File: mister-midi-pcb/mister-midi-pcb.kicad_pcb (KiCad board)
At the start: 2 copper layers, 106.9 x 68.6 mm, 31 parts, among them J1 Midi In, J2 USB3_A, J3 Midi Out, J4 Midi Thru, U1 H11L1, U2 74HC14, U3 LM1117-3.3

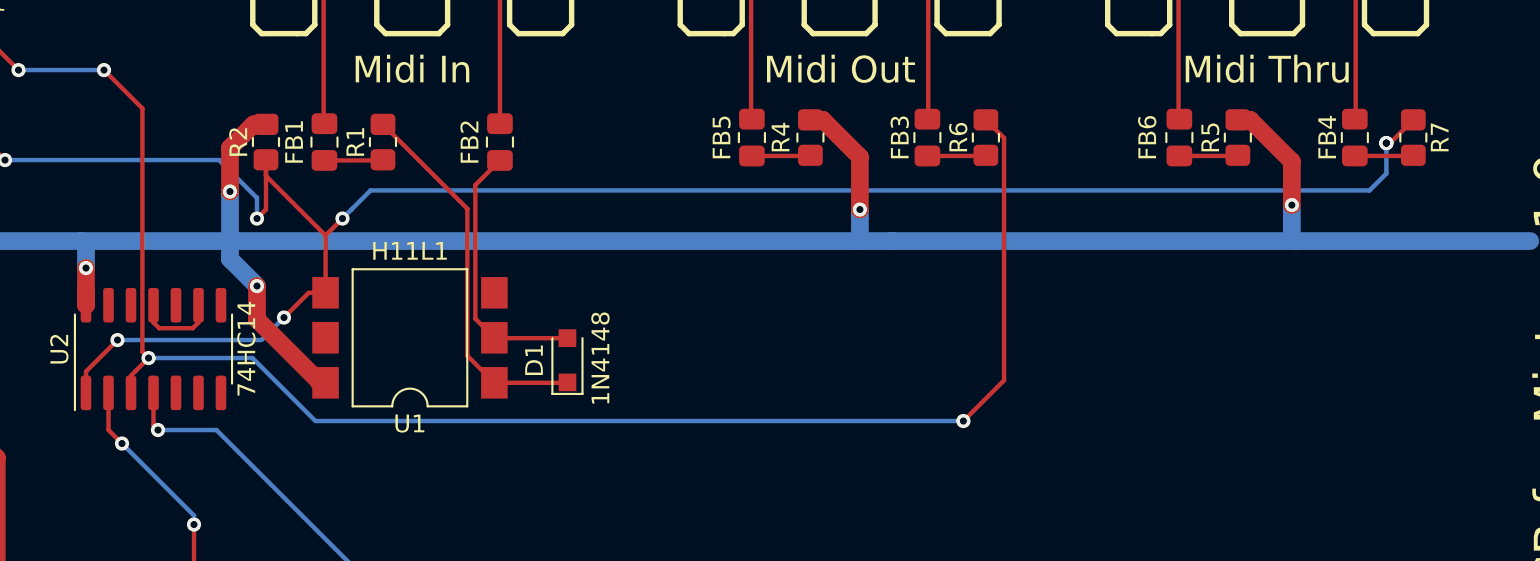
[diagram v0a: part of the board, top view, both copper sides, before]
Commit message: out and thru go through buffer now.
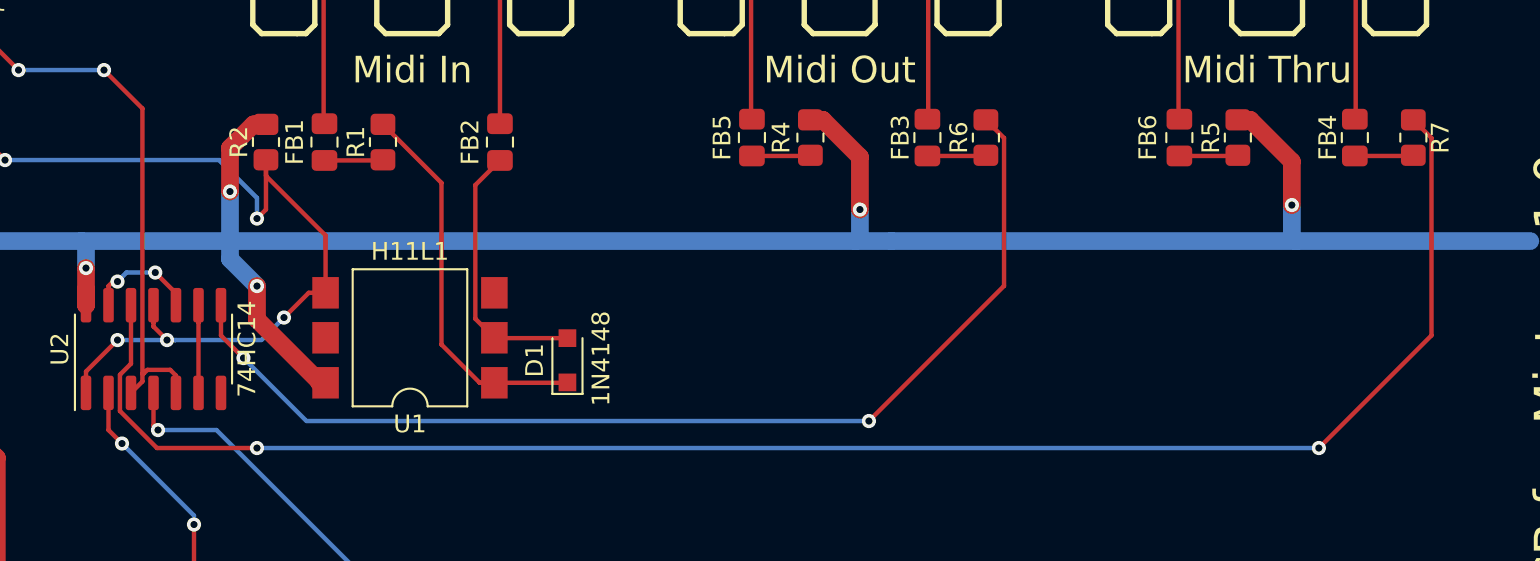
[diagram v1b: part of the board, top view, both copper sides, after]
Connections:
- R6 pad 1: Midi_Out_TX -> Net-(R6-Pad1)
- R7 pad 2: Midi_In_RX -> Net-(R7-Pad2)
- U2 pad 11: GND -> Midi_In_RX
- U2 pad 12: Net-(U2-Pad12) -> Net-(R7-Pad2)
- U2 pad 13: GND -> Net-(U2-Pad10)
- U2 pad 5: GND -> Midi_Out_TX
- U2 pad 8: Net-(U2-Pad8) -> Net-(R6-Pad1)
- U2 pad 9: GND -> Net-(U2-Pad6)
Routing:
- net Net-(R7-Pad2): track 0.00 -> 96.4 mm, vias 0 -> 2
- net Midi_Out_TX: track 101.0 -> 37.9 mm, vias 4 -> 2
- net Midi_In_RX: track 126.6 -> 65.2 mm, vias 7 -> 5
- net Net-(R6-Pad1): track 0.00 -> 60.9 mm, vias 0 -> 2
- net Net-(U2-Pad10): track 0.00 -> 7.19 mm, vias 0 -> 2
- net Net-(U2-Pad6): track 0.00 -> 5.92 mm
- net GND: track 4.76 -> 0.00 mm

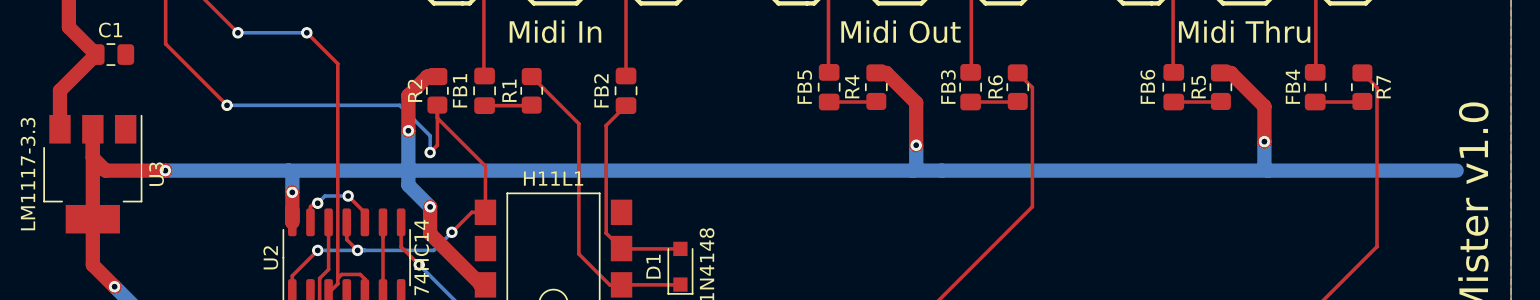
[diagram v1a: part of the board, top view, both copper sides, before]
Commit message: small trace improvements.
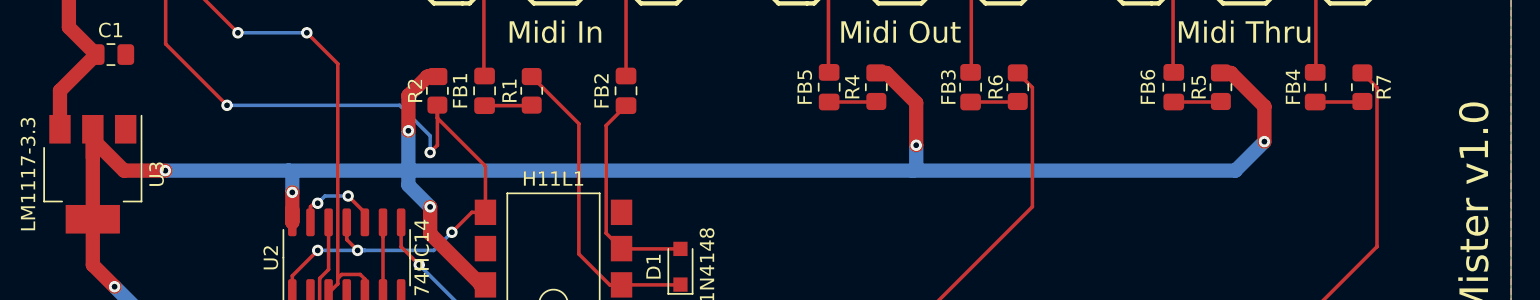
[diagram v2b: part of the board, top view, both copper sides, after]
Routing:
- net +3V3: track 182.0 -> 168.5 mm

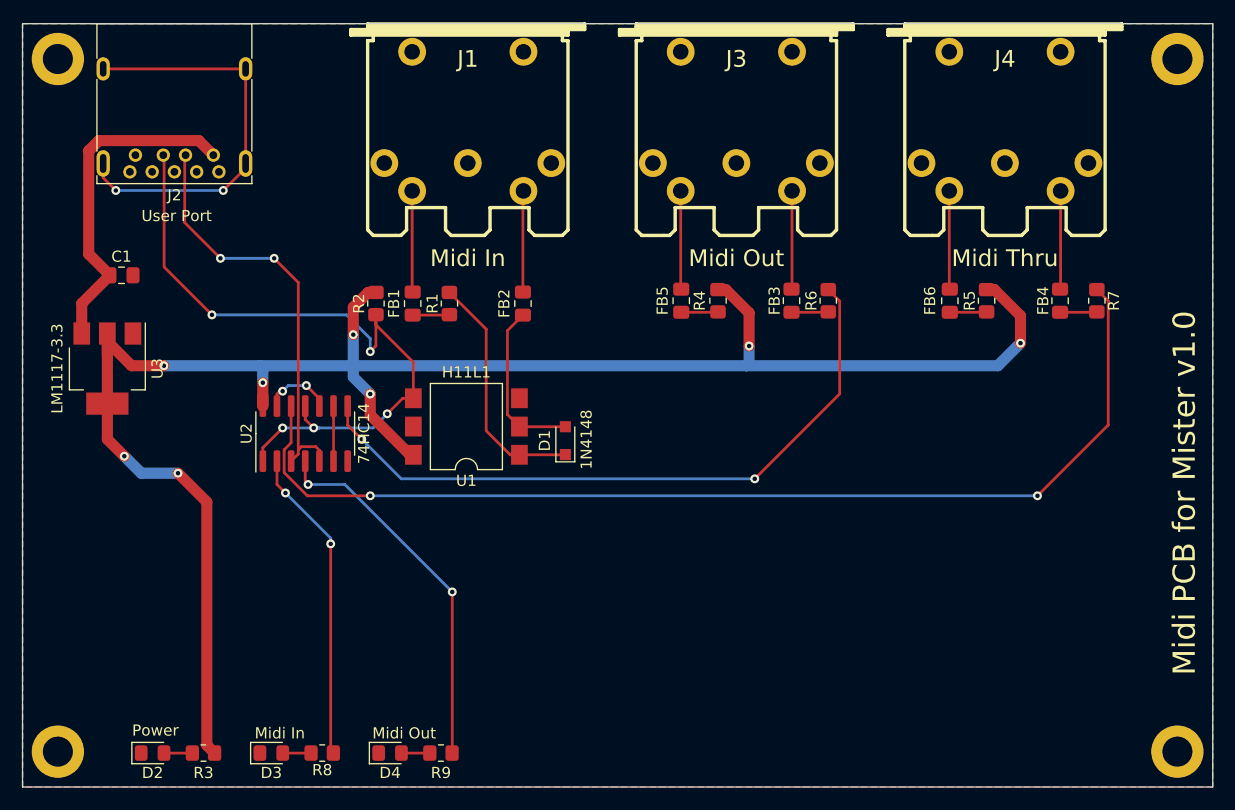
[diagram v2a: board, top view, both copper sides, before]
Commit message: added capacitors for ldo
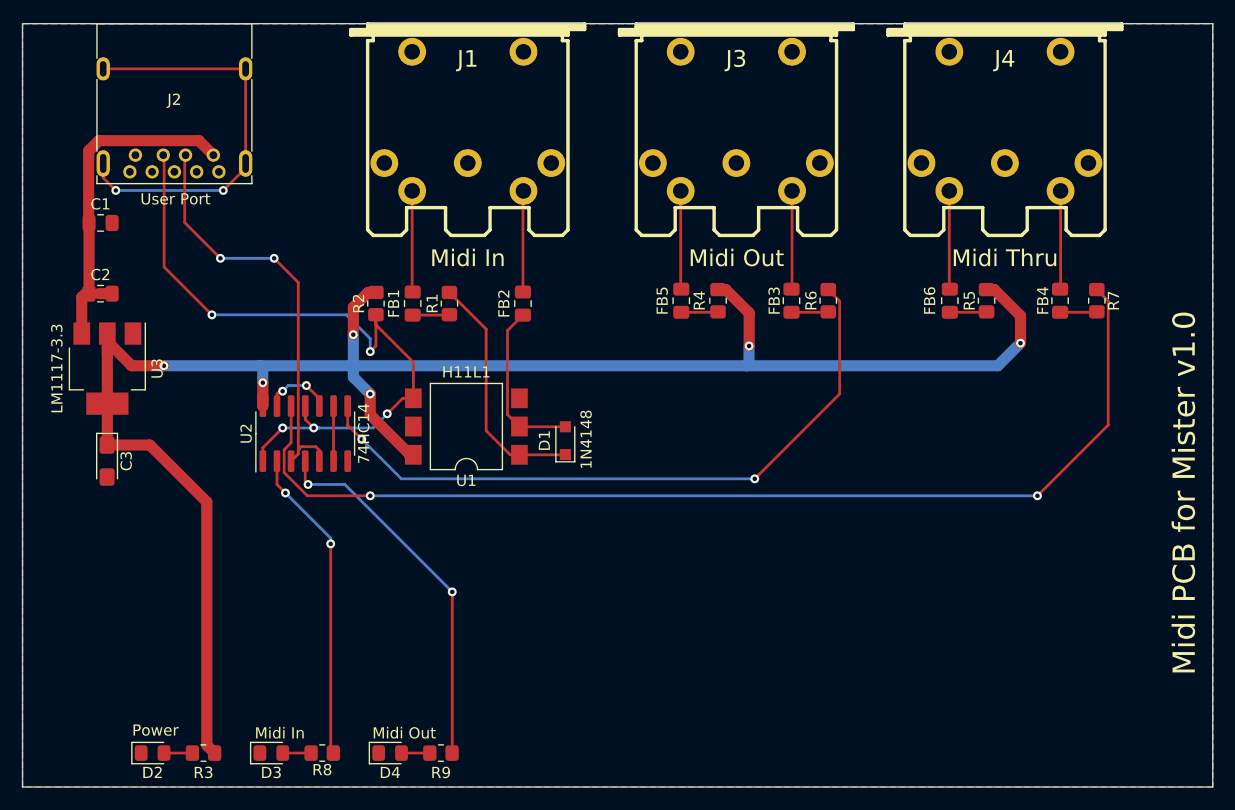
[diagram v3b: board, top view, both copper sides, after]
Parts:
- removed REF** (x4): MountingHole_2.7mm_M2.5_DIN965_Pad, MountingHole:MountingHole_2.7mm_M2.5_DIN965_Pad
- added C2: 10uF, Capacitor_SMD:C_0805_2012Metric_Pad1.18x1.45mm_HandSolder, F.Cu at (68.0, 100.5)
- added C3: 10uF, Capacitor_Tantalum_SMD:CP_EIA-3216-18_Kemet-A_Pad1.58x1.35mm_HandSolder, F.Cu at (68.6, 115.5)
- moved C1 5.06 mm to (68.0, 94.1)
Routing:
- net +5V: track 30.4 -> 27.8 mm
- net GND: track 0.00 -> 0.76 mm
- net +3V3: track 168.5 -> 168.8 mm, vias 8 -> 6

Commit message: updated gerbers, holes were missing.
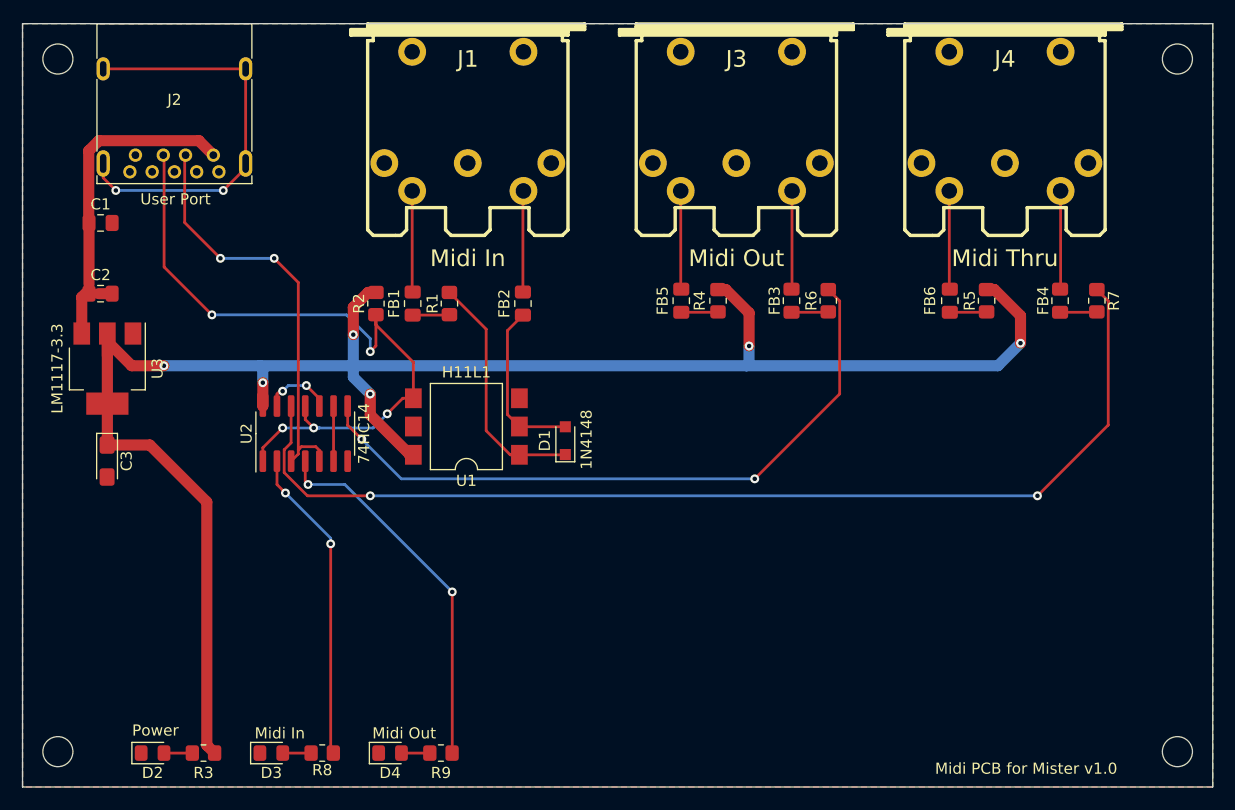
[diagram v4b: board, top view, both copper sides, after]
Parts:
- added REF**: MountingHole_2.7mm_M2.5_ISO7380, MountingHole:MountingHole_2.7mm_M2.5_ISO7380, F.Cu at (164.7, 141.6)
- added REF**: MountingHole_2.7mm_M2.5_ISO7380, MountingHole:MountingHole_2.7mm_M2.5_ISO7380, F.Cu at (64.1, 141.6)
- added REF**: MountingHole_2.7mm_M2.5_ISO7380, MountingHole:MountingHole_2.7mm_M2.5_ISO7380, F.Cu at (64.1, 79.4)
- added REF**: MountingHole_2.7mm_M2.5_ISO7380, MountingHole:MountingHole_2.7mm_M2.5_ISO7380, F.Cu at (164.7, 79.4)

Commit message: Fix #2,#3
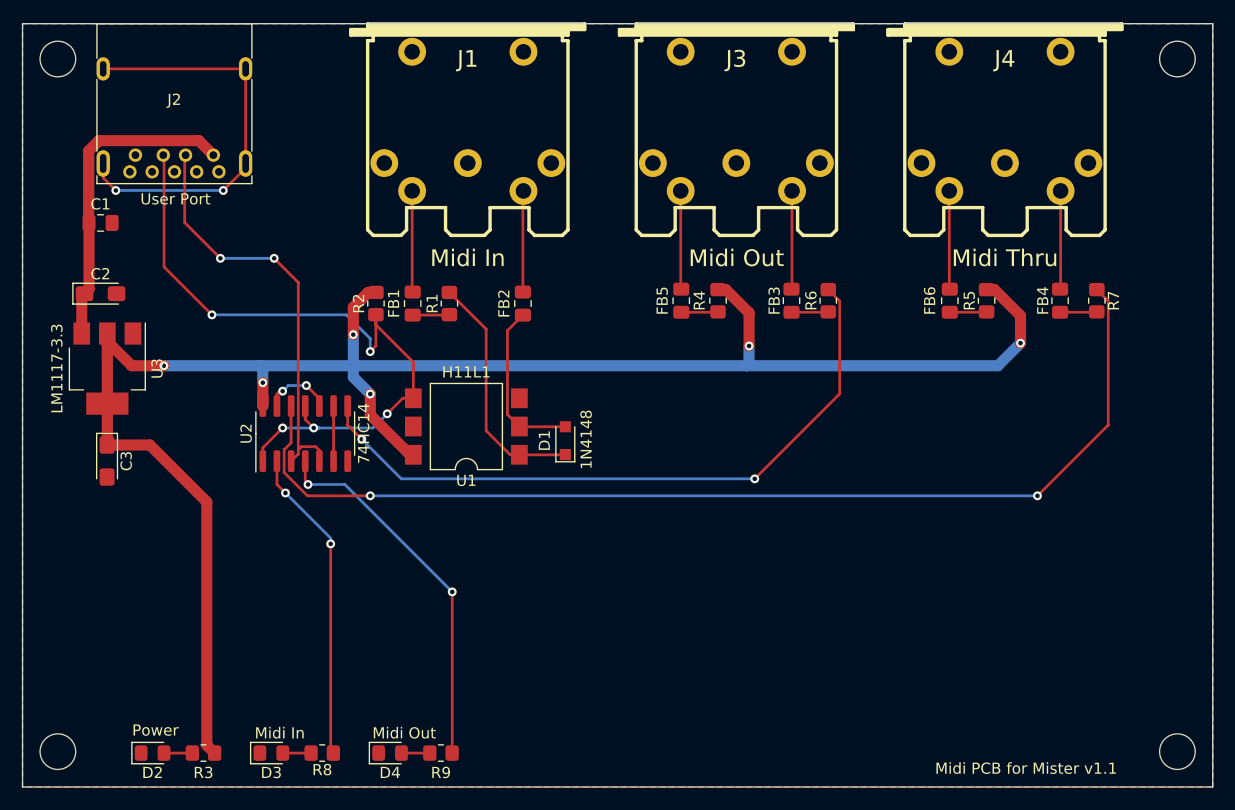
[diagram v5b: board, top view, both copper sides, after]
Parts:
- removed the REF** at (164.7, 141.6)
- removed the REF** at (64.1, 141.6)
- removed the REF** at (64.1, 79.4)
- removed the REF** at (164.7, 79.4)
- added REF**: MountingHole_3.2mm_M3_ISO7380, MountingHole:MountingHole_3.2mm_M3_ISO7380, F.Cu at (164.7, 79.4)
- added REF**: MountingHole_3.2mm_M3_ISO7380, MountingHole:MountingHole_3.2mm_M3_ISO7380, F.Cu at (164.7, 141.6)
- added REF**: MountingHole_3.2mm_M3_ISO7380, MountingHole:MountingHole_3.2mm_M3_ISO7380, F.Cu at (64.1, 141.6)
- added REF**: MountingHole_3.2mm_M3_ISO7380, MountingHole:MountingHole_3.2mm_M3_ISO7380, F.Cu at (64.1, 79.4)
- C2: footprint Capacitor_SMD:C_0805_2012Metric_Pad1.18x1.45mm_HandSolder -> Capacitor_Tantalum_SMD:CP_EIA-3216-18_Kemet-A_Pad1.58x1.35mm_HandSolder
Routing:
- net +5V: track 27.8 -> 28.8 mm
- net GND: track 0.76 -> 0.00 mm
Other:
- board text added: "Midi PCB for Mister v1.1"
- board text removed: "Midi PCB for Mister v1.0"

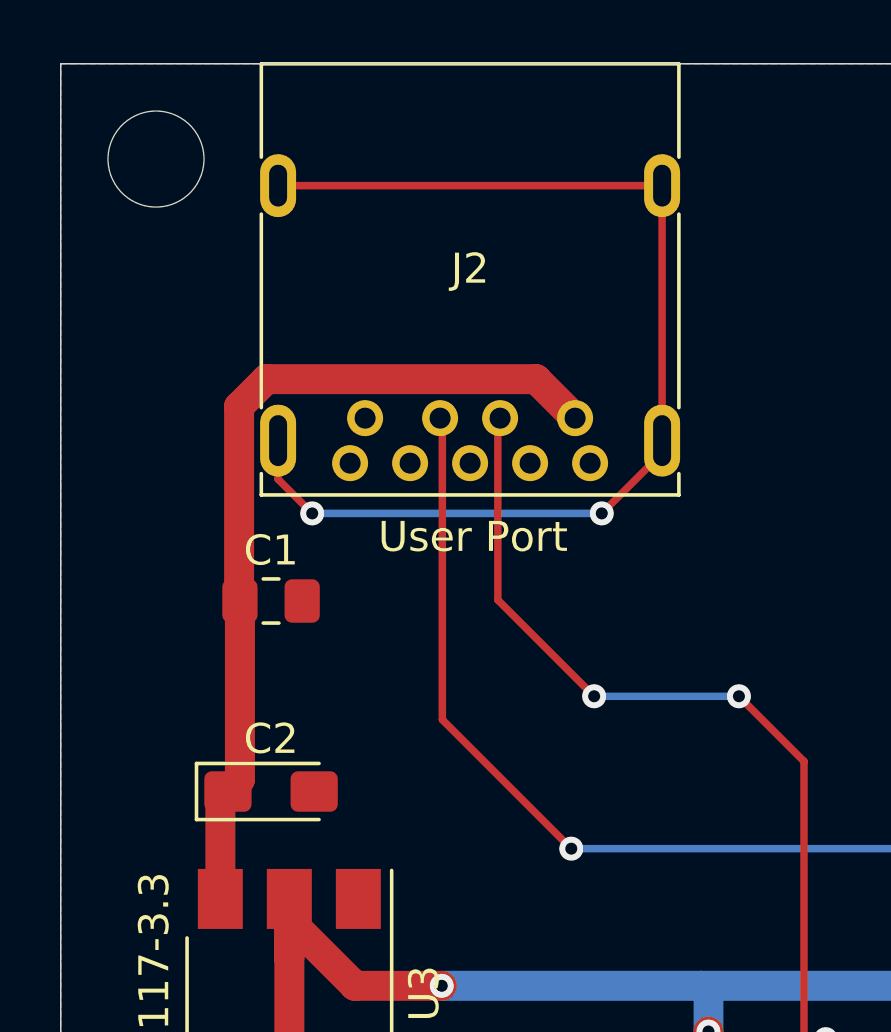
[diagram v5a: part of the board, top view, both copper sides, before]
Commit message: v1.1 of the midi pcb. fixed a couple of problems from the first prototype board.
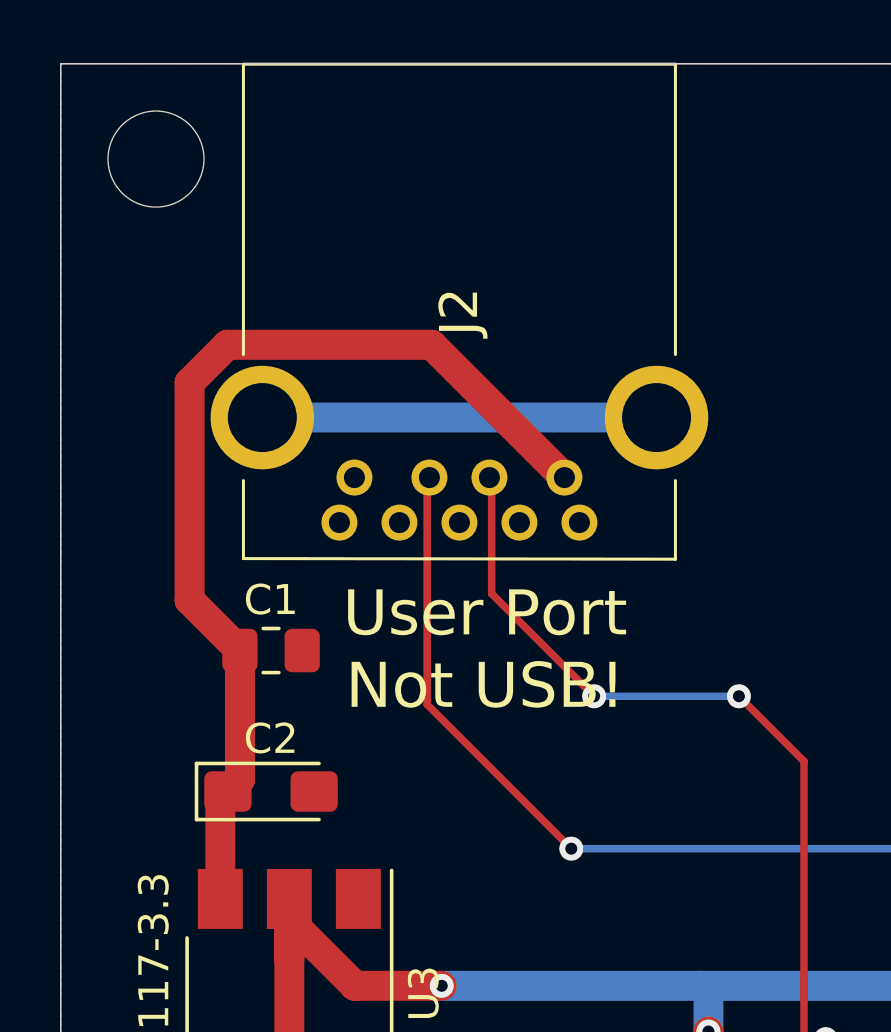
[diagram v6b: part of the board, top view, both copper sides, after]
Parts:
- J2: footprint Connector_USB:USB3_A_Molex_48393-001 -> samacsys:GSB3111113HR
- REF** (x4): value MountingHole_3.2mm_M3_ISO7380 -> MountingHole_3.2mm_M3_mini; footprint MountingHole:MountingHole_3.2mm_M3_ISO7380 -> samacsys:MountingHole_3.2mm_M3_mini
- moved J2 2.01 mm to (77.7, 90.0), turned to 270 degrees
- moved C1 1.65 mm to (68.0, 95.8)
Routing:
- net Net-(J2-Pad10): track 37.1 -> 13.1 mm, vias 2 -> 0
- net +5V: track 28.8 -> 33.1 mm
- net Midi_Out_TX: track 37.9 -> 36.0 mm
- net Midi_In_RX: track 65.2 -> 63.4 mm
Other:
- board text added: "User Port Not USB!"
- board text removed: "User Port"
